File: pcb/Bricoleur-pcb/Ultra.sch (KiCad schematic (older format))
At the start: 3 parts, among them U1 Ultrasonic-LV-EZ0, U3 Ultrasonic-LV-EZ0, U4 Ultrasonic-LV-EZ0

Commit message: PCB…
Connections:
- net PYNQ_3V3 renamed VMCU
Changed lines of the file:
@@
 $Descr A4 11693 8268
 encoding utf-8
-Sheet 7 18
+Sheet 6 18
 Title ""
 Date ""
@@
 	0    -1   1    0
 $EndComp
-Text Label 4850 3350 0    50   ~ 0
-GND
-Text Label 4850 3250 0    50   ~ 0
-PYNQ_3V3
 $Comp
 L Bricoleur-pcb-rescue:Bricoleur-pcb-cache_Ultrasonic-LV-EZ0-Bricoleur-pcb-cache U?
@@
 	0    -1   1    0
 $EndComp
-Text Label 4850 4150 0    50   ~ 0
-PYNQ_3V3
-Text Label 4850 5050 0    50   ~ 0
-PYNQ_3V3
-Text Label 4850 4250 0    50   ~ 0
-GND
-Text Label 4850 5150 0    50   ~ 0
-GND
 Text GLabel 4850 2850 2    50   Input ~ 0
 PULSE
@@
 Wire Wire Line
 	5650 2400 5300 2400
+Text GLabel 4850 3250 2    50   Input ~ 0
+VMCU
+Text GLabel 5100 4450 2    50   Input ~ 0
+VMCU
+Text GLabel 4850 4150 2    50   Input ~ 0
+VMCU
+Text GLabel 4850 5050 2    50   Input ~ 0
+VMCU
+Text GLabel 4850 3350 2    50   Input ~ 0
+GND
+Text GLabel 4850 4250 2    50   Input ~ 0
+GND
+Text GLabel 4850 5150 2    50   Input ~ 0
+GND
 $EndSCHEMATC

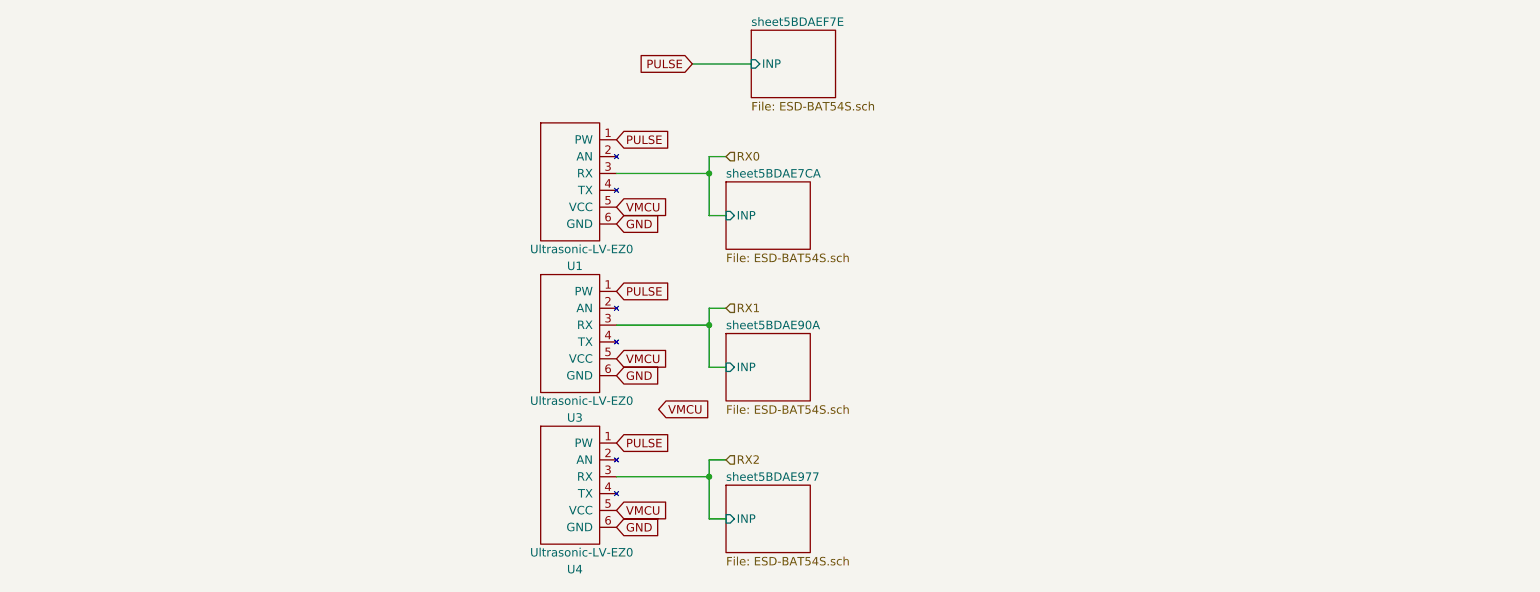
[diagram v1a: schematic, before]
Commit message: Cleanup, labeling, schematic size reduction
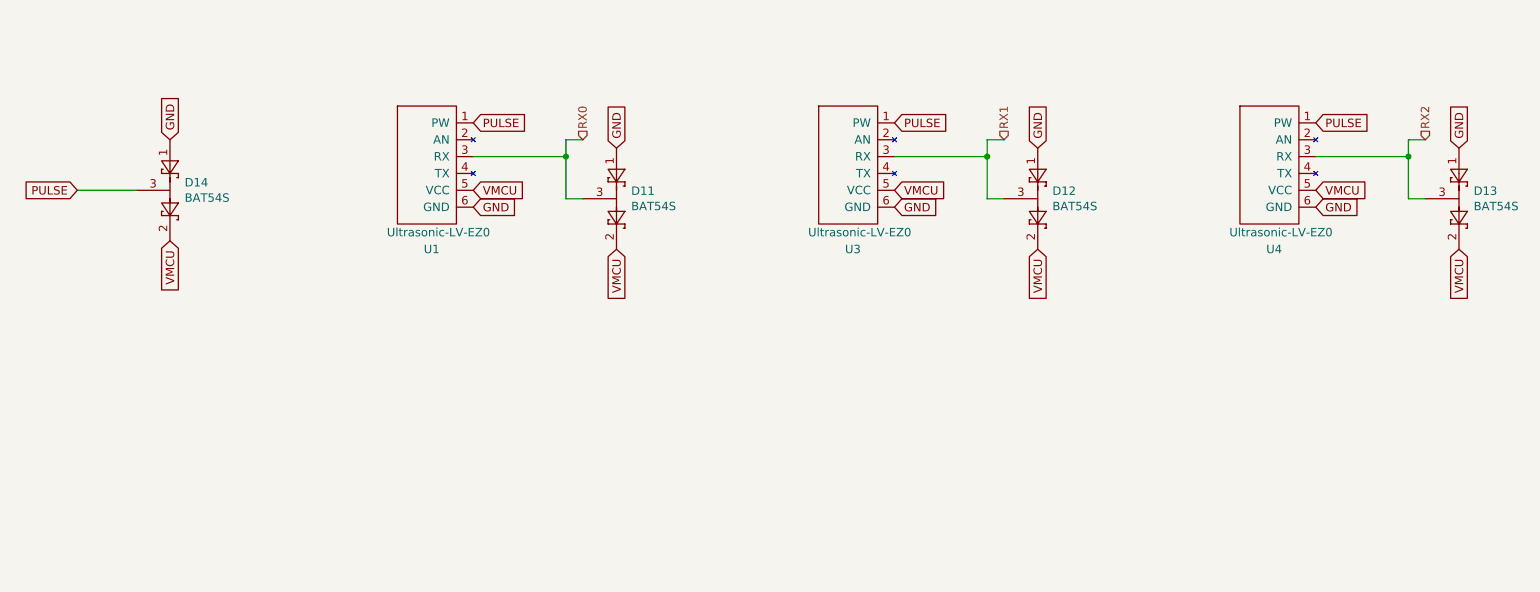
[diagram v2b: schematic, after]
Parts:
- added D11, D12, D13, D14: BAT54S, Package_TO_SOT_SMD:SOT-23, symbol Diode:BAT54S
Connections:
- net GND: now also D11.1, D12.1, D13.1, D14.1
- net PULSE: now also D14.3
- net RX0: now also D11.3
- net RX1: now also D12.3
- net RX2: now also D13.3
- net VMCU: now also D11.2, D12.2, D13.2, D14.2
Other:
- moved on the sheet: U1, U3, U4
